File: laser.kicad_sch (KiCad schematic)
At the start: 15 parts, among them J3 Conn_Coaxial, Q1 BC547, Q2 BC547, U6 LM317_TO-220, U7 LM317_TO-220

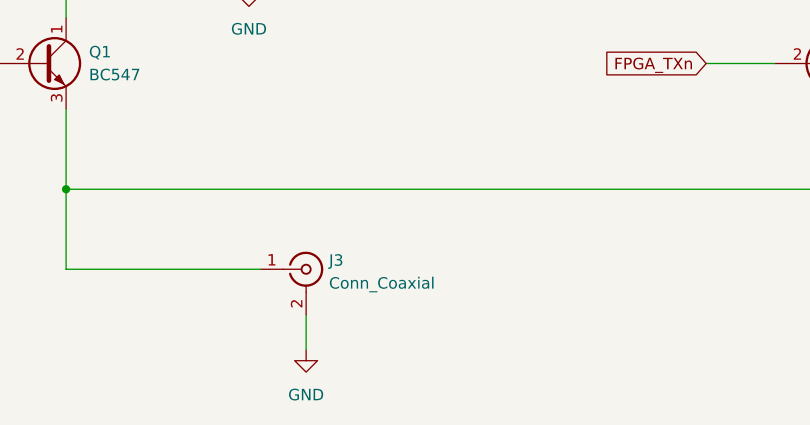
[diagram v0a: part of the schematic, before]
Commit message: Add SMA connector footprint and assign source
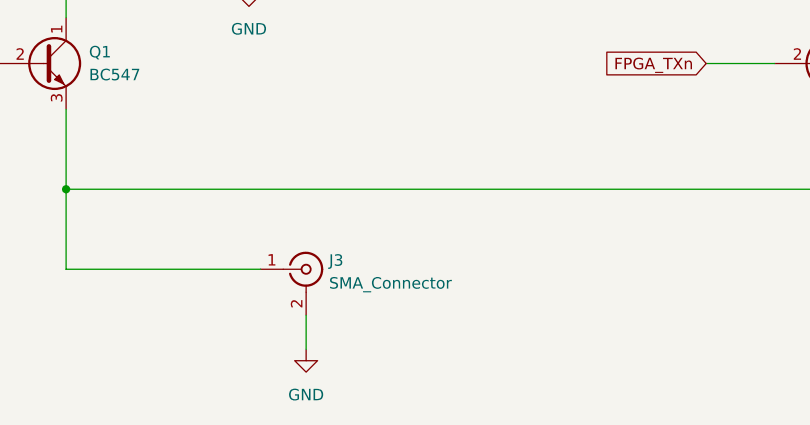
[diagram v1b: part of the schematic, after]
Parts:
- J3: value Conn_Coaxial -> SMA_Connector; footprint Connector_Coaxial:SMA_Amphenol_901-144_Vertical -> SMA Connector:733910070; Source (none) -> https://onecall.farnell.com/molex/73391-0070/rf-coax-conn-s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
- Q1, Q2: Source (none) -> L7 store
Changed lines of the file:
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@@
       (effects (font (size 1.27 1.27)) (justify left))
     )
-    (property "Value" "Conn_Coaxial" (id 1) (at 134.62 112.0531 0)
+    (property "Value" "SMA_Connector" (id 1) (at 134.62 112.0531 0)
       (effects (font (size 1.27 1.27)) (justify left))
     )
-    (property "Footprint" "Connector_Coaxial:SMA_Amphenol_901-144_Vertical" (id 2) (at 132.08 110.49 0)
+    (property "Footprint" "SMA Connector:733910070" (id 2) (at 132.08 110.49 0)
       (effects (font (size 1.27 1.27)) hide)
     )
     (property "Datasheet" " ~" (id 3) (at 132.08 110.49 0)
+      (effects (font (size 1.27 1.27)) hide)
+    )
+    (property "Source" "https://onecall.farnell.com/molex/73391-0070/rf-coax-conn-sma-jack-50-ohm-pcb/dp/1909301" (id 4) (at 132.08 110.49 0)
       (effects (font (size 1.27 1.27)) hide)
     )
@@
       (effects (font (size 1.27 1.27)) (justify left) hide)
     )
+    (property "Source" "L7 store" (id 4) (at 102.87 87.63 0)
+      (effects (font (size 1.27 1.27)) hide)
+    )
     (pin "1")
     (pin "2")
@@
       (effects (font (size 1.27 1.27)) (justify left) hide)
     )
+    (property "Source" "L7 store" (id 4) (at 189.23 87.63 0)
+      (effects (font (size 1.27 1.27)) hide)
+    )
     (pin "1")

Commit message: Add inductor footprints
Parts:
- U6, U7: Source (none) -> L7 store
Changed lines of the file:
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@@
+      (effects (font (size 1.27 1.27)) hide)
+    )
+    (property "Source" "L7 store" (id 4) (at 63.5 46.99 0)
       (effects (font (size 1.27 1.27)) hide)
     )
@@
       (effects (font (size 1.27 1.27)) hide)
     )
+    (property "Source" "L7 store" (id 4) (at 148.59 46.99 0)
+      (effects (font (size 1.27 1.27)) hide)
+    )

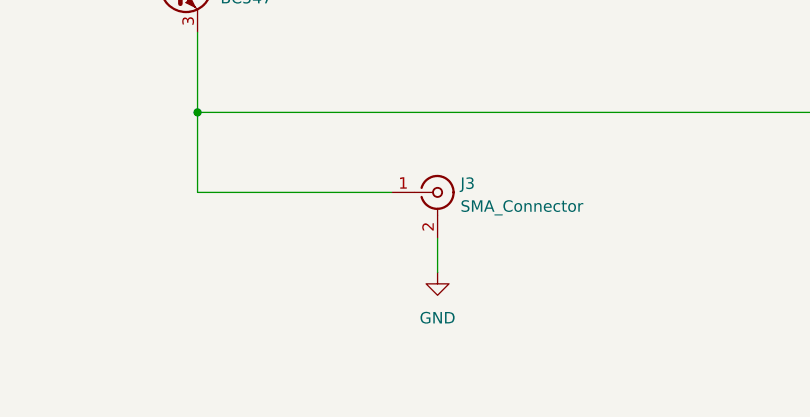
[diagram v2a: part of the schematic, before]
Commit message: Change SMA connector symbol to match footprint
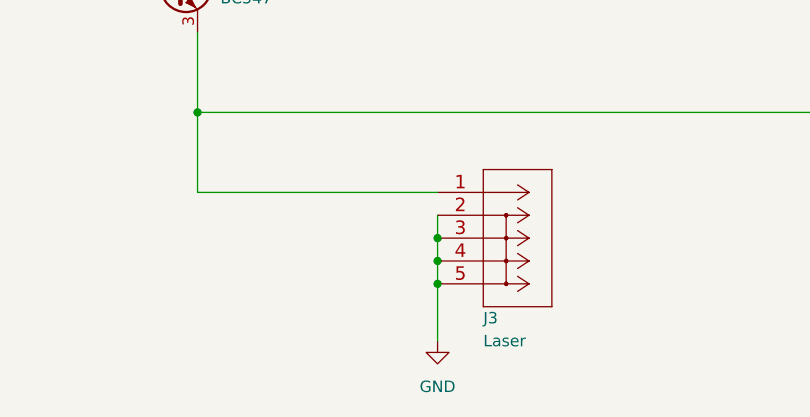
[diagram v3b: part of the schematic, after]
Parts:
- J3: value SMA_Connector -> Laser; footprint SMA Connector:733910070 -> CONN_73391-0070_MOL; symbol Connector:Conn_Coaxial -> SMA_Connector:733910070
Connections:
- net GND: now also J3.3, J3.4, J3.5
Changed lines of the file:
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@@
 (kicad_sch (version 20211123) (generator eeschema)
   (paper "A4")
+  (junction (at 132.08 115.57) (diameter 0) (color 0 0 0 0)
+  )
   (junction (at 125.73 46.99) (diameter 0) (color 0 0 0 0)
   )
@@
   (junction (at 165.1 46.99) (diameter 0) (color 0 0 0 0)
   )
+  (junction (at 132.08 118.11) (diameter 0) (color 0 0 0 0)
+  )
   (junction (at 165.1 78.74) (diameter 0) (color 0 0 0 0)
   )
@@
   (junction (at 176.53 46.99) (diameter 0) (color 0 0 0 0)
   )
+  (junction (at 132.08 120.65) (diameter 0) (color 0 0 0 0)
+  )
   (junction (at 186.69 46.99) (diameter 0) (color 0 0 0 0)
   )
@@
     (stroke (width 0) (type default) (color 0 0 0 0))
   )
-  (wire (pts (xy 105.41 110.49) (xy 127 110.49))
+  (wire (pts (xy 105.41 110.49) (xy 132.08 110.49))
     (stroke (width 0) (type default) (color 0 0 0 0))
   )
@@
     (stroke (width 0) (type default) (color 0 0 0 0))
   )
+  (wire (pts (xy 132.08 118.11) (xy 132.08 120.65))
+    (stroke (width 0) (type default) (color 0 0 0 0))
+  )
   (wire (pts (xy 165.1 78.74) (xy 176.53 78.74))
     (stroke (width 0) (type default) (color 0 0 0 0))
   )
+  (wire (pts (xy 132.08 115.57) (xy 132.08 118.11))
+    (stroke (width 0) (type default) (color 0 0 0 0))
+  )
   (wire (pts (xy 105.41 101.6) (xy 105.41 110.49))
     (stroke (width 0) (type default) (color 0 0 0 0))
@@
     (stroke (width 0) (type default) (color 0 0 0 0))
   )
-  (wire (pts (xy 132.08 119.38) (xy 132.08 115.57))
+  (wire (pts (xy 132.08 113.03) (xy 132.08 115.57))
     (stroke (width 0) (type default) (color 0 0 0 0))
   )
@@
   )
   (wire (pts (xy 80.01 46.99) (xy 91.44 46.99))
+    (stroke (width 0) (type default) (color 0 0 0 0))
+  )
+  (wire (pts (xy 132.08 120.65) (xy 132.08 127))
     (stroke (width 0) (type default) (color 0 0 0 0))
   )
@@
     (pin "2")
   )
-  (symbol (lib_id "Connector:Conn_Coaxial") (at 132.08 110.49 0) (unit 1)
-    (in_bom yes) (on_board yes) (fields_autoplaced)
-    (property "Reference" "J3" (id 0) (at 134.62 109.5131 0)
-      (effects (font (size 1.27 1.27)) (justify left))
-    )
-    (property "Value" "SMA_Connector" (id 1) (at 134.62 112.0531 0)
-      (effects (font (size 1.27 1.27)) (justify left))
-    )
-    (property "Footprint" "SMA Connector:733910070" (id 2) (at 132.08 110.49 0)
-      (effects (font (size 1.27 1.27)) hide)
+  (symbol (lib_id "SMA_Connector:733910070") (at 132.08 110.49 0) (unit 1)
+    (in_bom yes) (on_board yes)
+    (property "Reference" "J3" (id 0) (at 137.16 124.46 0)
+      (effects (font (size 1.27 1.27)) (justify left))
+    )
+    (property "Value" "Laser" (id 1) (at 137.16 127 0)
+      (effects (font (size 1.27 1.27)) (justify left))
+    )
+    (property "Footprint" "CONN_73391-0070_MOL" (id 2) (at 142.24 117.094 0)
+      (effects (font (size 1.524 1.524)) hide)
     )
     (property "Datasheet" " ~" (id 3) (at 132.08 110.49 0)
@@
     (pin "1")
     (pin "2")
+    (pin "3")
+    (pin "4")
+    (pin "5")
   )
   (symbol (lib_id "Device:C") (at 91.44 50.8 0) (unit 1)
@@
     (pin "2")
   )
-  (symbol (lib_id "power:GND") (at 132.08 119.38 0) (unit 1)
-    (in_bom yes) (on_board yes) (fields_autoplaced)
-    (property "Reference" "#PWR021" (id 0) (at 132.08 125.73 0)
-      (effects (font (size 1.27 1.27)) hide)
-    )
-    (property "Value" "GND" (id 1) (at 132.08 124.46 0))
-    (property "Footprint" "" (id 2) (at 132.08 119.38 0)
-      (effects (font (size 1.27 1.27)) hide)
-    )
-    (property "Datasheet" "" (id 3) (at 132.08 119.38 0)
-      (effects (font (size 1.27 1.27)) hide)
-    )
+  (symbol (lib_id "power:GND") (at 132.08 127 0) (unit 1)
+    (in_bom yes) (on_board yes) (fields_autoplaced)
+    (property "Reference" "#PWR021" (id 0) (at 132.08 133.35 0)
+      (effects (font (size 1.27 1.27)) hide)
+    )
+    (property "Value" "GND" (id 1) (at 132.08 132.08 0))
+    (property "Footprint" "" (id 2) (at 132.08 127 0)
+      (effects (font (size 1.27 1.27)) hide)
+    )
+    (property "Datasheet" "" (id 3) (at 132.08 127 0)
+      (effects (font (size 1.27 1.27)) hide)
+    )

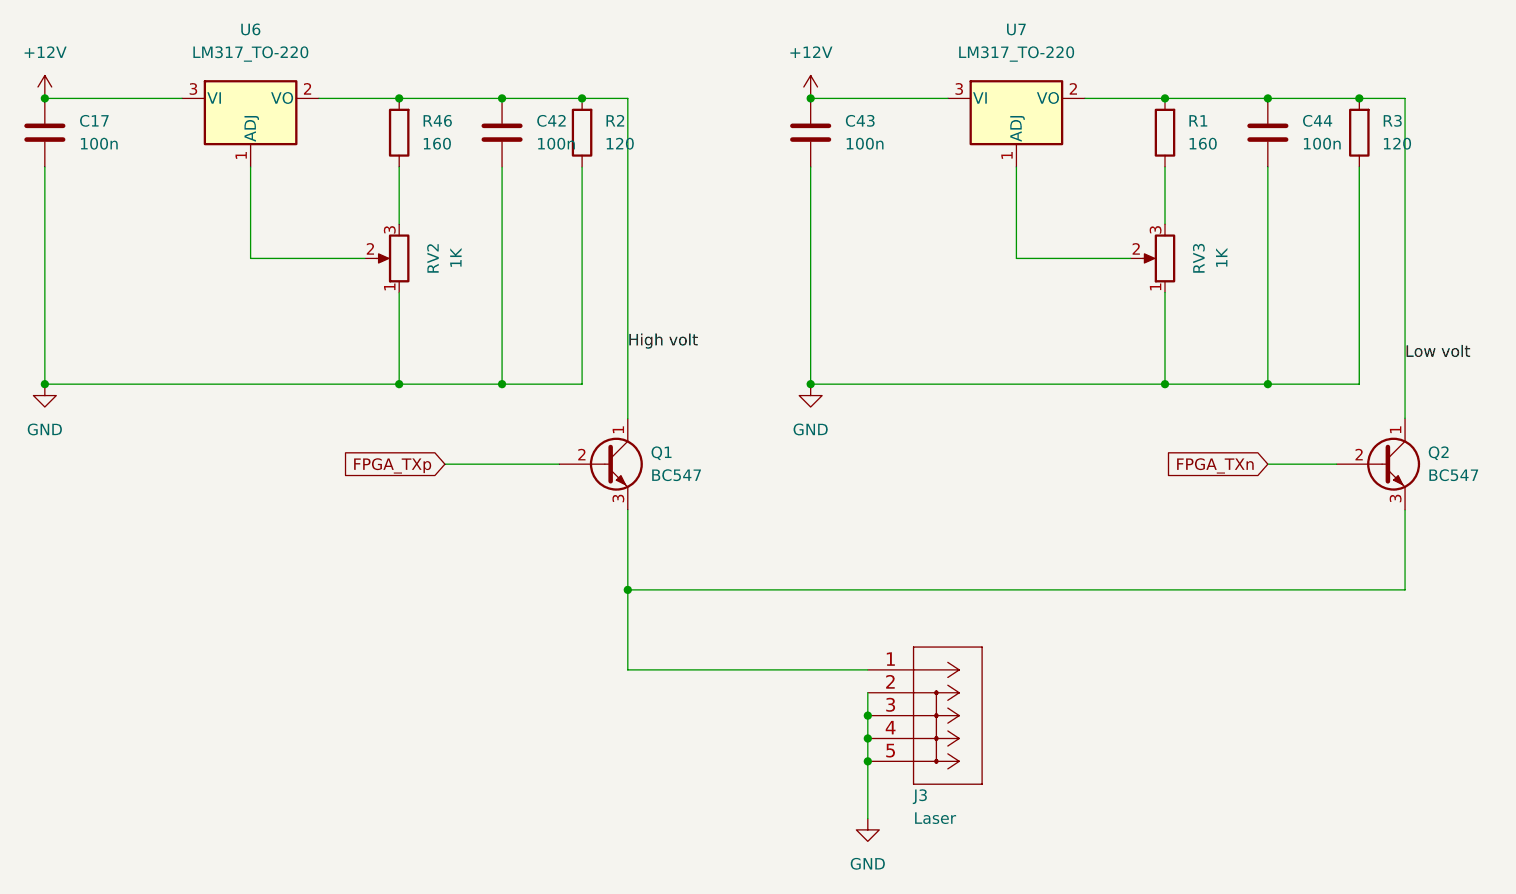
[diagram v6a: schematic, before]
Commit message: tweaked power circuit, sorted drc errors and warnings, visual checked pcb
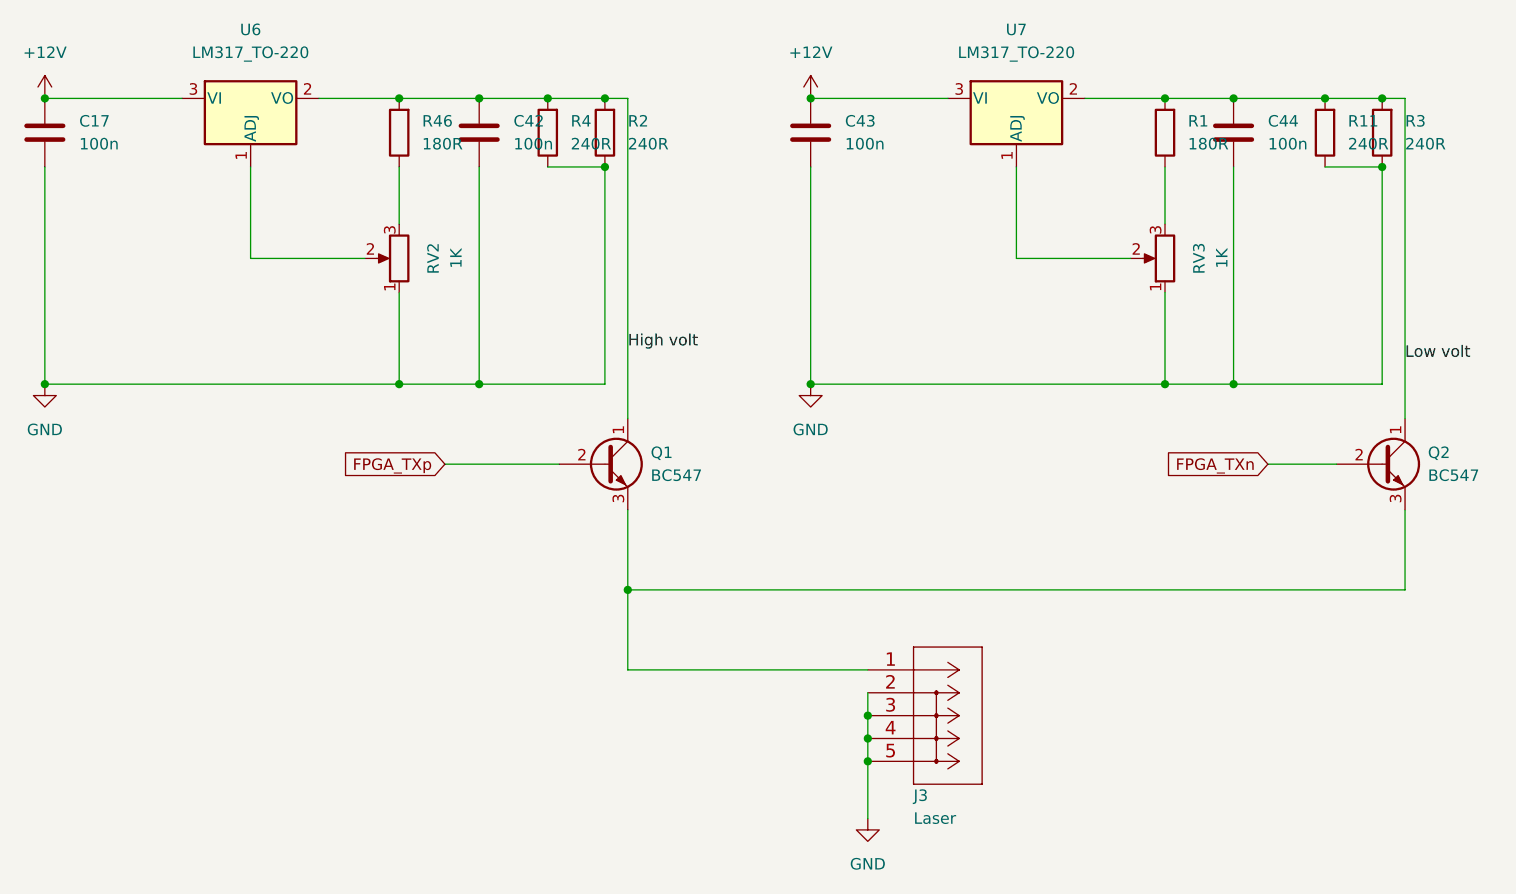
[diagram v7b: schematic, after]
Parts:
- added R11, R4: 240R, Resistor_THT:R_Axial_DIN0207_L6.3mm_D2.5mm_P10.16mm_Horizontal, symbol Device:R
- J3: footprint CONN_73391-0070_MOL -> SMA Connector:733910070
- R1, R46: value 160 -> 180R; Source (none) -> L3 Store
- R2, R3: value 120 -> 240R; footprint Resistor_SMD:R_0805_2012Metric_Pad1.20x1.40mm_HandSolder -> Resistor_THT:R_Axial_DIN0207_L6.3mm_D2.5mm_P10.16mm_Horizontal; Source (none) -> L7 Store
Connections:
- net GND: now also R11.1, R4.1
- net High volt: now also R4.2
- net Low volt: now also R11.2
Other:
- moved on the sheet: C42, C44, R2, R3

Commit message: more design review and added ground planes
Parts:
- RV2, RV3: Source https://onecall.farnell.com/vishay/t93yb104kt20/trimmer-pot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 -> L7 store
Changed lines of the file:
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@@
       (effects (font (size 1.27 1.27)) hide)
     )
-    (property "Source" "https://onecall.farnell.com/vishay/t93yb104kt20/trimmer-pot-100k-23turn-thd/dp/1141422" (id 4) (at 165.1 64.77 0)
+    (property "Source" "L7 store" (id 4) (at 165.1 64.77 0)
       (effects (font (size 1.27 1.27)) hide)
     )
@@
       (effects (font (size 1.27 1.27)) hide)
     )
-    (property "Source" "https://onecall.farnell.com/vishay/t93yb104kt20/trimmer-pot-100k-23turn-thd/dp/1141422" (id 4) (at 80.01 64.77 0)
+    (property "Source" "L7 store" (id 4) (at 80.01 64.77 0)
       (effects (font (size 1.27 1.27)) hide)
     )
